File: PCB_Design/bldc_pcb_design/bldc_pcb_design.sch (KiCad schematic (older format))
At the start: 49 parts, among them IC1 DRV8305NPHPR, J1 Conn_01x04_Female, SW1 BOOT, SW2 RESET, U1 ESP32-WROOM-32D, U2 BSC022N04LS6ATMA1, U3 BSC022N04LS6ATMA1, U4 BSC022N04LS6ATMA1, U5 BSC022N04LS6ATMA1, U6 BSC022N04LS6ATMA1, U7 BSC022N04LS6ATMA1, U8 AS5600-ASOT, U9 LM2672M-3.3

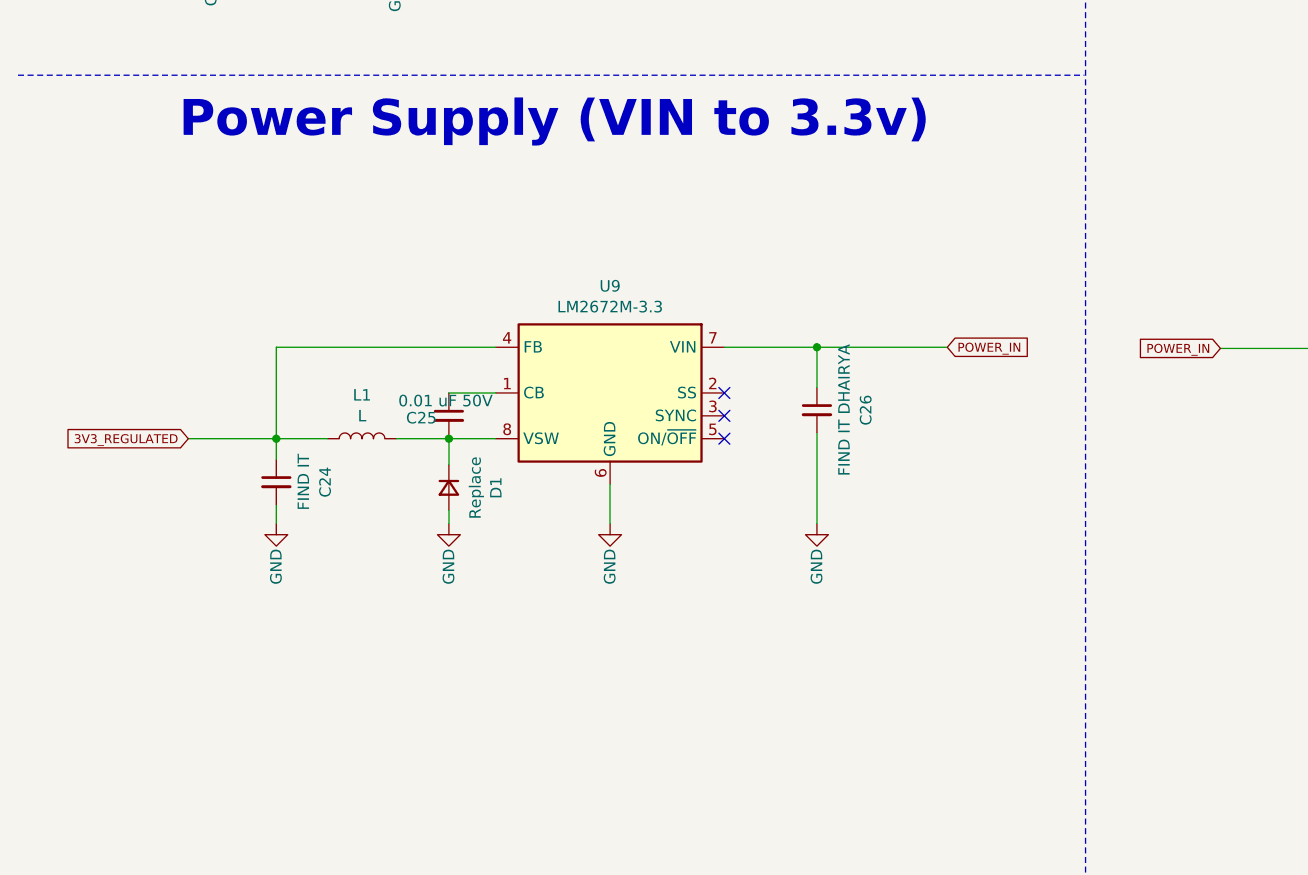
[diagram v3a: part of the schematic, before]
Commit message: Added component values for buck converter
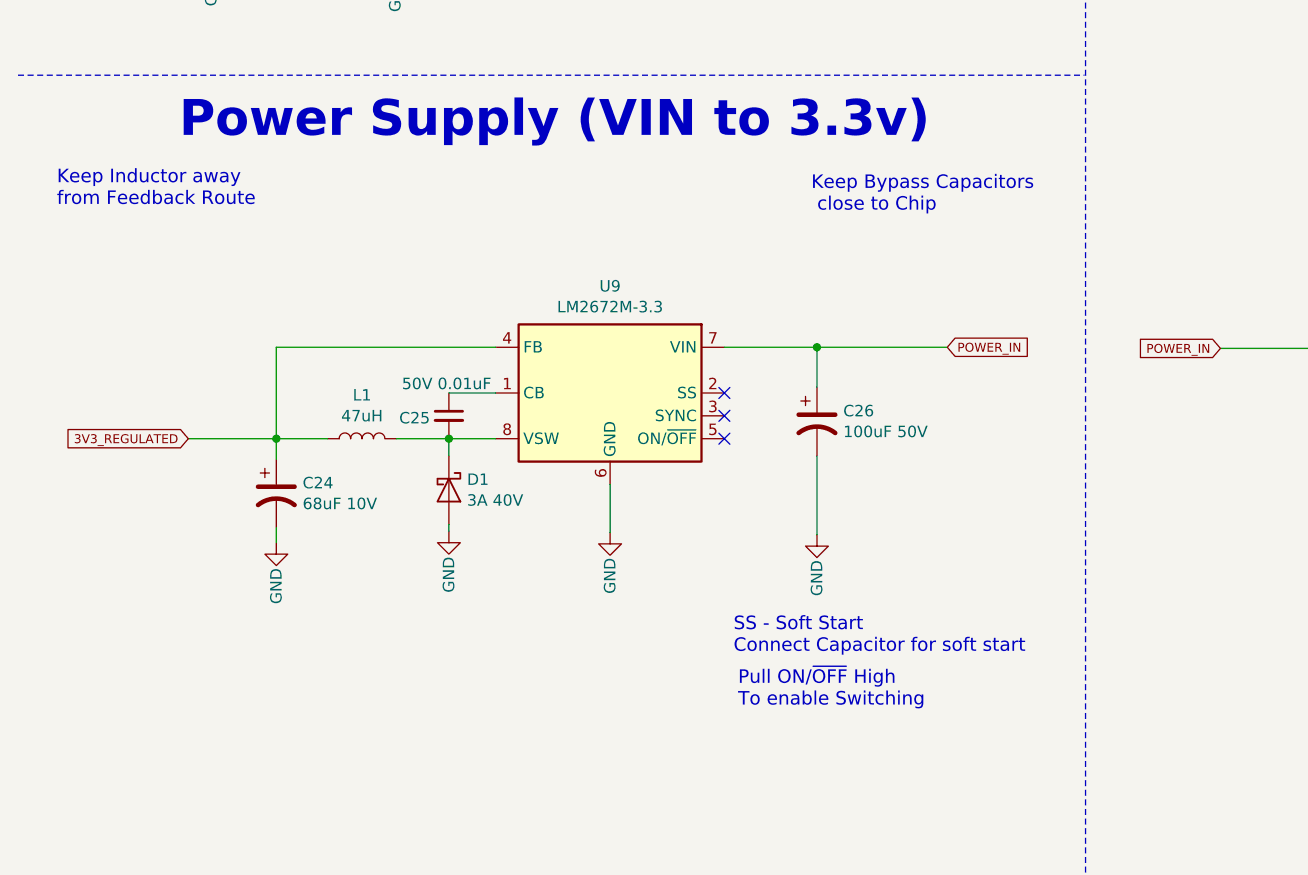
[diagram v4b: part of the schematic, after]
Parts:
- removed C24: FIND IT, symbol Device:C_Small
- removed C26: FIND IT DHAIRYA, symbol Device:C_Small
- removed D1: Replace, symbol Device:D_Small
- added C24: 68uF 10V, symbol Device:CP1
- added C26: 100uF 50V, symbol Device:CP1
- added D1: 3A 40V, symbol Device:D_Schottky
- C25: value 0.01 uF 50V -> 50V 0.01uF
- L1: value L -> 47uH
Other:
- note added: "Keep Bypass Capacitors\n close to Chip"
- note added: "Keep Inductor away \nfrom Feedback Route"
- note added: "Pull ON/~OFF~ High\nTo enable Switching"
- note added: "SS - Soft Start\nConnect Capacitor for soft start"
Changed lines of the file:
@@
 L power:GND #PWR021
 U 1 1 61396B76
-P 3075 9250
-F 0 "#PWR021" H 3075 9000 50  0001 C CNN
-F 1 "GND" V 3075 9060 50  0000 C CNN
-F 2 "" H 3075 9250 50  0001 C CNN
-F 3 "" H 3075 9250 50  0001 C CNN
-	1    3075 9250
+P 3075 9290
+F 0 "#PWR021" H 3075 9040 50  0001 C CNN
+F 1 "GND" V 3075 9100 50  0000 C CNN
+F 2 "" H 3075 9290 50  0001 C CNN
+F 3 "" H 3075 9290 50  0001 C CNN
+	1    3075 9290
 	1    0    0    -1
 $EndComp
@@
 Wire Wire Line
 	5745 8485 7050 8485
-$Comp
-L Device:C_Small C26
-U 1 1 614136E9
-P 3980 8755
-F 0 "C26" V 4195 8755 50  0000 C CNN
-F 1 "FIND IT DHAIRYA" V 4100 8755 50  0000 C CNN
-F 2 "" H 3980 8755 50  0001 C CNN
-F 3 "~" H 3980 8755 50  0001 C CNN
-	1    3980 8755
-	1    0    0    -1
-$EndComp
 Wire Wire Line
 	3980 8655 3980 8480
@@
 L power:GND #PWR022
 U 1 1 61425A4E
-P 3980 9250
-F 0 "#PWR022" H 3980 9000 50  0001 C CNN
-F 1 "GND" V 3980 9060 50  0000 C CNN
-F 2 "" H 3980 9250 50  0001 C CNN
-F 3 "" H 3980 9250 50  0001 C CNN
-	1    3980 9250
+P 3980 9300
+F 0 "#PWR022" H 3980 9050 50  0001 C CNN
+F 1 "GND" V 3980 9110 50  0000 C CNN
+F 2 "" H 3980 9300 50  0001 C CNN
+F 3 "" H 3980 9300 50  0001 C CNN
+	1    3980 9300
 	1    0    0    -1
 $EndComp
@@
 U 1 1 6143826A
 P 2370 8780
-F 0 "C25" H 2250 8770 50  0000 C CNN
-F 1 "0.01 uF 50V" H 2355 8845 50  0000 C CNN
+F 0 "C25" H 2220 8770 50  0000 C CNN
+F 1 "50V 0.01uF " H 2360 8920 50  0000 C CNN
 F 2 "" H 2370 8780 50  0001 C CNN
 F 3 "~" H 2370 8780 50  0001 C CNN
@@
 	1    0    0    -1
 $EndComp
-$Comp
-L Device:C_Small C24
-U 1 1 6143855F
-P 1615 9070
-F 0 "C24" V 1830 9070 50  0000 C CNN
-F 1 "FIND IT" V 1735 9070 50  0000 C CNN
-F 2 "" H 1615 9070 50  0001 C CNN
-F 3 "~" H 1615 9070 50  0001 C CNN
-	1    1615 9070
-	1    0    0    -1
-$EndComp
-$Comp
-L Device:D_Small D1
-U 1 1 6143D556
-P 2370 9095
-F 0 "D1" H 2370 9302 50  0000 C CNN
-F 1 "Replace" H 2370 9211 50  0000 C CNN
-F 2 "" V 2370 9095 50  0001 C CNN
-F 3 "~" V 2370 9095 50  0001 C CNN
-	1    2370 9095
-	0    1    1    0
-$EndComp
 Text GLabel 1230 8880 0    39   Input ~ 0
 3V3_REGULATED
 Wire Wire Line
-	3980 8855 3980 9250
+	3980 8955 3980 9300
 Wire Wire Line
-	3075 9080 3075 9250
+	3075 9080 3075 9290
 $Comp
 L power:GND #PWR019
 U 1 1 614ACA2E
-P 1615 9250
-F 0 "#PWR019" H 1615 9000 50  0001 C CNN
-F 1 "GND" V 1615 9060 50  0000 C CNN
-F 2 "" H 1615 9250 50  0001 C CNN
-F 3 "" H 1615 9250 50  0001 C CNN
-	1    1615 9250
+P 1615 9335
+F 0 "#PWR019" H 1615 9085 50  0001 C CNN
+F 1 "GND" V 1615 9145 50  0000 C CNN
+F 2 "" H 1615 9335 50  0001 C CNN
+F 3 "" H 1615 9335 50  0001 C CNN
+	1    1615 9335
 	1    0    0    -1
 $EndComp
-Wire Wire Line
-	1615 9170 1615 9250
 Wire Wire Line
 	1615 8970 1615 8880
@@
 L power:GND #PWR020
 U 1 1 61562ED3
-P 2370 9250
-F 0 "#PWR020" H 2370 9000 50  0001 C CNN
-F 1 "GND" V 2370 9060 50  0000 C CNN
-F 2 "" H 2370 9250 50  0001 C CNN
-F 3 "" H 2370 9250 50  0001 C CNN
-	1    2370 9250
+P 2370 9285
+F 0 "#PWR020" H 2370 9035 50  0001 C CNN
+F 1 "GND" V 2370 9095 50  0000 C CNN
+F 2 "" H 2370 9285 50  0001 C CNN
+F 3 "" H 2370 9285 50  0001 C CNN
+	1    2370 9285
 	1    0    0    -1
 $EndComp
 Wire Wire Line
-	2370 8995 2370 8880
+	2370 8955 2370 8880
 Wire Wire Line
-	2370 9195 2370 9250
+	2370 9255 2370 9285
 $Comp
 L Device:L L1
@@
 P 1990 8880
 F 0 "L1" V 2180 8880 50  0000 C CNN
-F 1 "L" V 2089 8880 50  0000 C CNN
+F 1 "47uH" V 2089 8880 50  0000 C CNN
 F 2 "" H 1990 8880 50  0001 C CNN
 F 3 "~" H 1990 8880 50  0001 C CNN
@@
 Wire Wire Line
 	1615 8480 1615 8880
+Text Notes 3955 7895 0    59   ~ 0
+Keep Bypass Capacitors\n close to Chip
+Text Notes 655  7870 0    59   ~ 0
+Keep Inductor away \nfrom Feedback Route
+Text Notes 3615 9825 0    59   ~ 0
+SS - Soft Start\nConnect Capacitor for soft start
+Text Notes 3635 10060 0    59   ~ 0
+Pull ON/~OFF~ High\nTo enable Switching
+$Comp
+L Device:D_Schottky D1
+U 1 1 613262EF
+P 2370 9105
+F 0 "D1" V 2324 9184 50  0000 L CNN
+F 1 "3A 40V" V 2415 9184 50  0000 L CNN
+F 2 "" H 2370 9105 50  0001 C CNN
+F 3 "~" H 2370 9105 50  0001 C CNN
+	1    2370 9105
+	0    1    1    0
+$EndComp
+$Comp
+L Device:CP1 C26
+U 1 1 6141F4E4
+P 3980 8805
+F 0 "C26" H 4095 8851 50  0000 L CNN
+F 1 "100uF 50V" H 4095 8760 50  0000 L CNN
+F 2 "" H 3980 8805 50  0001 C CNN
+F 3 "~" H 3980 8805 50  0001 C CNN
+	1    3980 8805
+	1    0    0    -1
+$EndComp
+$Comp
+L Device:CP1 C24
+U 1 1 614AC597
+P 1615 9120
+F 0 "C24" H 1730 9166 50  0000 L CNN
+F 1 "68uF 10V" H 1730 9075 50  0000 L CNN
+F 2 "" H 1615 9120 50  0001 C CNN
+F 3 "~" H 1615 9120 50  0001 C CNN
+	1    1615 9120
+	1    0    0    -1
+$EndComp
+Wire Wire Line
+	1615 9270 1615 9335
 $EndSCHEMATC

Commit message: Added schematics for DRV8305
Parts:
- removed C11, C13, C14, C15: 100nF, symbol Device:C
- removed C16: 10uF, symbol Device:C
- removed C19, C5, C7: C, symbol Device:C
- removed C24: 68uF 10V, symbol Device:CP1
- removed C26: 100uF 50V, symbol Device:CP1
- removed R1: 100k, symbol Device:R
- removed R6, R7: R, symbol Device:R
- removed U2, U3, U4, U5, U6, U7: BSC022N04LS6ATMA1, PG-TDSON-8-6_INF, symbol BSC022N04LS6ATMA1:BSC022N04LS6ATMA1
- added C?: 4.7uF Ceramic, symbol Device:C
- added C? (x2): 0.047uF, symbol Device:C
- added C?: 100uF 100V, symbol Device:C
- added C?: 68uF 10V, symbol Device:C
- added R? (x2): 10k, symbol Device:R
- added U? (x6): CSD18532NQ5B, DNK8, symbol CSD18532NQ5B:CSD18532NQ5B
- C1, C2, C3: value 1uF -> 1uF 6.3V
- C10: value 1uF -> 1uF 16V
- C9: value 2.2uF -> 2.2uF 16V
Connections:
- net labels added: DRV_HG_reg, DRV_LG_reg, DRV_SPI_CLK, DRV_SPI_MISO, DRV_SPI_MOSI, DRV_SPI_nSCS, PWR_GD, SO1, SO2, SO3
- net labels removed: 3V3, DRV_SO1, DRV_SO2, DRV_SO3, DRV_WAKE, DRV_nSCS, SPI_MISO, SPI_MOSI, SPI_SCLK_INT, VCPH, VCP_LSD, VOLT_MON
- wire segments 237 -> 219
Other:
- note added: "5-V internal analog supply \nregulator bypass capacitor"
- note added: "Connect with-> 3.3V or 5V, 50-mA LDO; \n connect 1-µF to GND\nConnect with-> Reference voltage; LDO disabled"
- note added: "DRV8305 - Gate Driver"
- note added: "DRV_DVDD: 3.3V internal digital\nsupply regulator"
- note added: "DRV_VREG: Internalamplifier \nreference voltage and SDO pullup."
- note added: "DRV_nFAULT: Fault\nIndicator"
- note added: "Flying capacitors for \ncharge pumps with rating :\nPVDD for CP1\nPVDD*2 for CP2"
- note added: "High Side MOSFET\nDrain"
- note added: "Input Voltage-\n8V to 40V"
- note added: "Output Voltage-\n3.3V 1A"
- note added: "PWRGD: Power Good\nDRV_VREG and MCU \nwatchdog fault \nindication"
- note added: "Power Bypass \nCapacitor"
- note added: "Pull ON/~OFF~ High\nTo enable Switching\nNC - Internal Default \nPull Up"
- note added: "SNP1, SN2 and SN3 are\nnegative current sense input pins\nfor amplifers 1,2 and 3 respectively\n"
- note added: "SO1, SO2 and SO3 are \ncurrent amplifier output pins\n"
- note added: "SP1, SP2 and SP3 are \npositive current sense input pins\nfor amplifers 1,2 and 3 respectively\n"
- note added: "VCPH - High Side Gate Driver regulator\nVCP_LSD - Low SIde Gate Driver regulator"
- note added: "do2014ac footprint"
- note removed: "Pull ON/~OFF~ High\nTo enable Switching"
- moved on the sheet: C1, C10, C12, C17, C18, C2, C3, C4, C6, C8, C9, IC1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

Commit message: Added TI Mosfets and LEDS
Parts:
- removed C17, C18: 1uF, symbol Device:C
- added C10, C11, C12, C13, C8: 1uF, symbol Device:C
- added D2, D3: LED, symbol Device:LED
- added R5: 10k, symbol Device:R
- added R7: 330, symbol Device:R
- gave numbers to parts that had none: 13
- renumbered C20 to C1, C4 to C15, C6 to C16, C8 to C17, C9 to C18, C2 to C19, C10 to C20, C1 to C21, C3 to C24, C25 to C3, C21 to C4, C22 to C5, C23 to C7, C12 to C9, R3 to R1, R4 to R2, R5 to R3, R8 to R4, R2 to R8, U8 to U2, U9 to U3
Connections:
- net 3V3_IN: now also D2.2 (A), D3.2 (A)
- net DRV_nFAULT: now also R7.2
- net GND: now also C10.2, C11.2, C12.2, C13.2, C8.2, R5.2
- net PVDD: now also C10.1, C11.1, C12.1, C13.1, C8.1
- new net: D3.1 (K), R7.1
- new net: D2.1 (K), R5.1
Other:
- note added: "3V3_ISOLATED is used to \npower ESP32 when board \nisn't being powered \nby VIN. (while programming)\n"
- note added: "Connect with-> \n3.3V or 5V, 50-mA LDO; \n connect 1-µF to GND\nReference voltage; LDO disabled"
- note added: "Magnetic Encoder (AS5600)"
- note added: "Power LED\n"
- note added: "TitanLegs"
- note removed: "3V3_ISOLATED is used to \npower ESP32 when board \nisn't being powered \nby VIN."
- note removed: "Connect with-> 3.3V or 5V, 50-mA LDO; \n connect 1-µF to GND\nConnect with-> Reference voltage; LDO disabled"
- note removed: "Magnetic Encoder"
- moved on the sheet: C19, C4, C5, C9, R6, R8, R9
